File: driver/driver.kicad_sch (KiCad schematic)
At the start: 16 parts, among them U1 ULN2003A, U2 ULN2003A, U3 74HC595, U4 74HC165

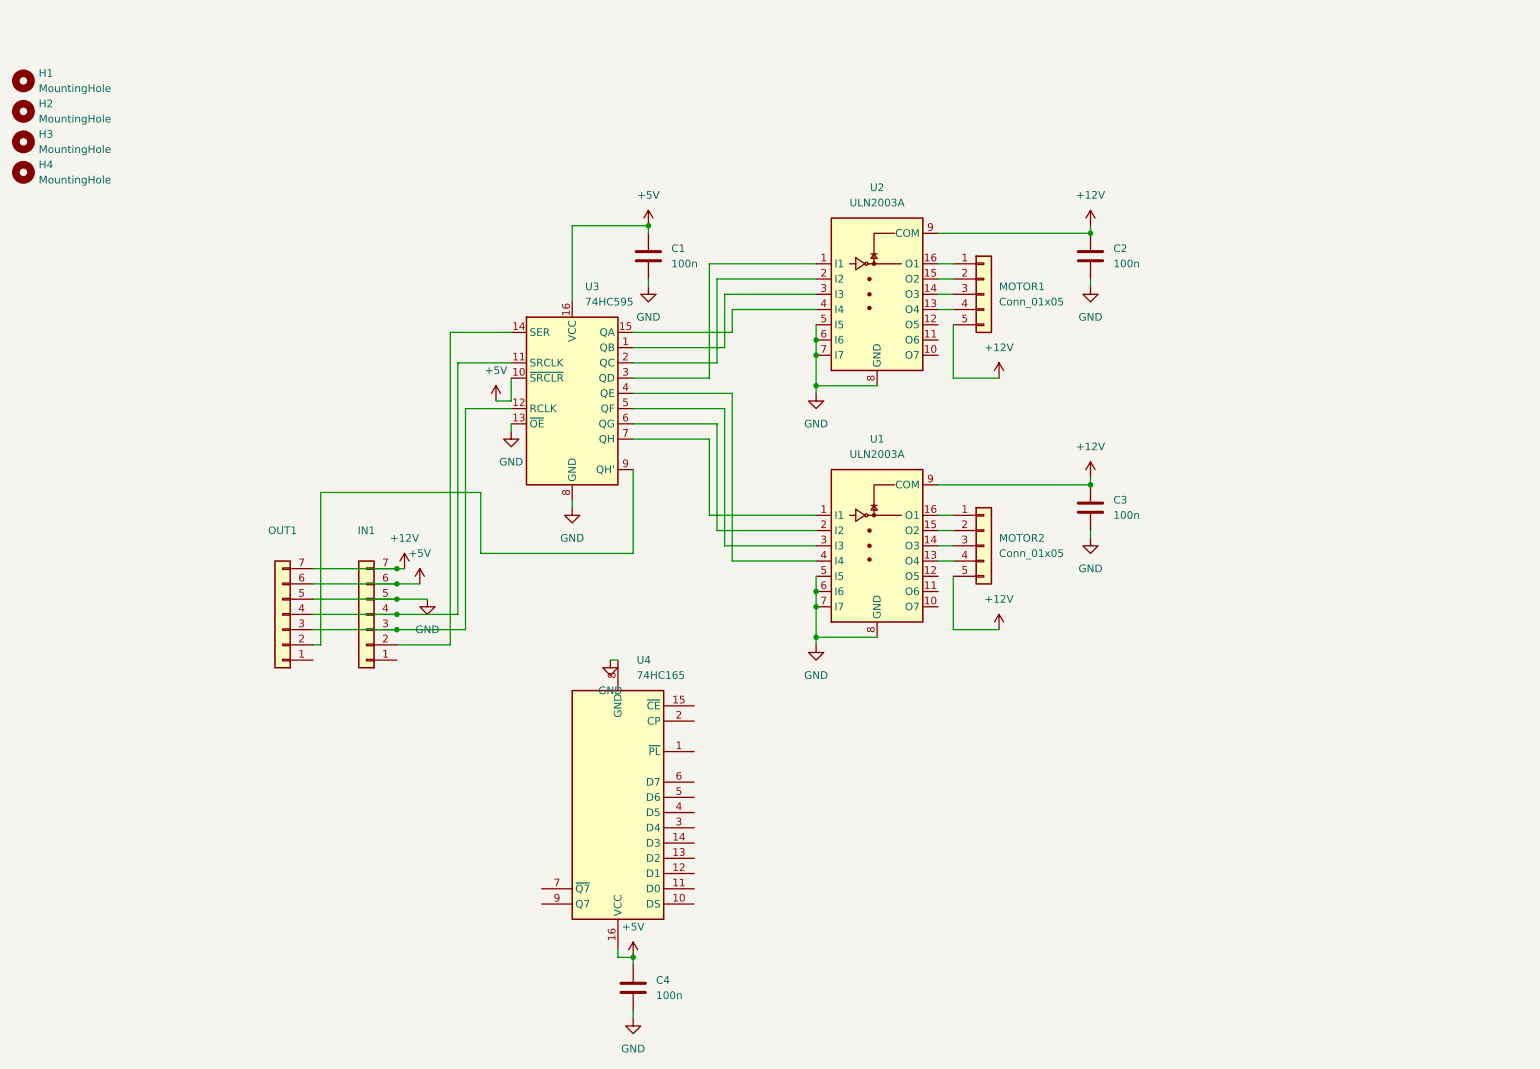
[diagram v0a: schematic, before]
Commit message: Start to implement controller and driver.
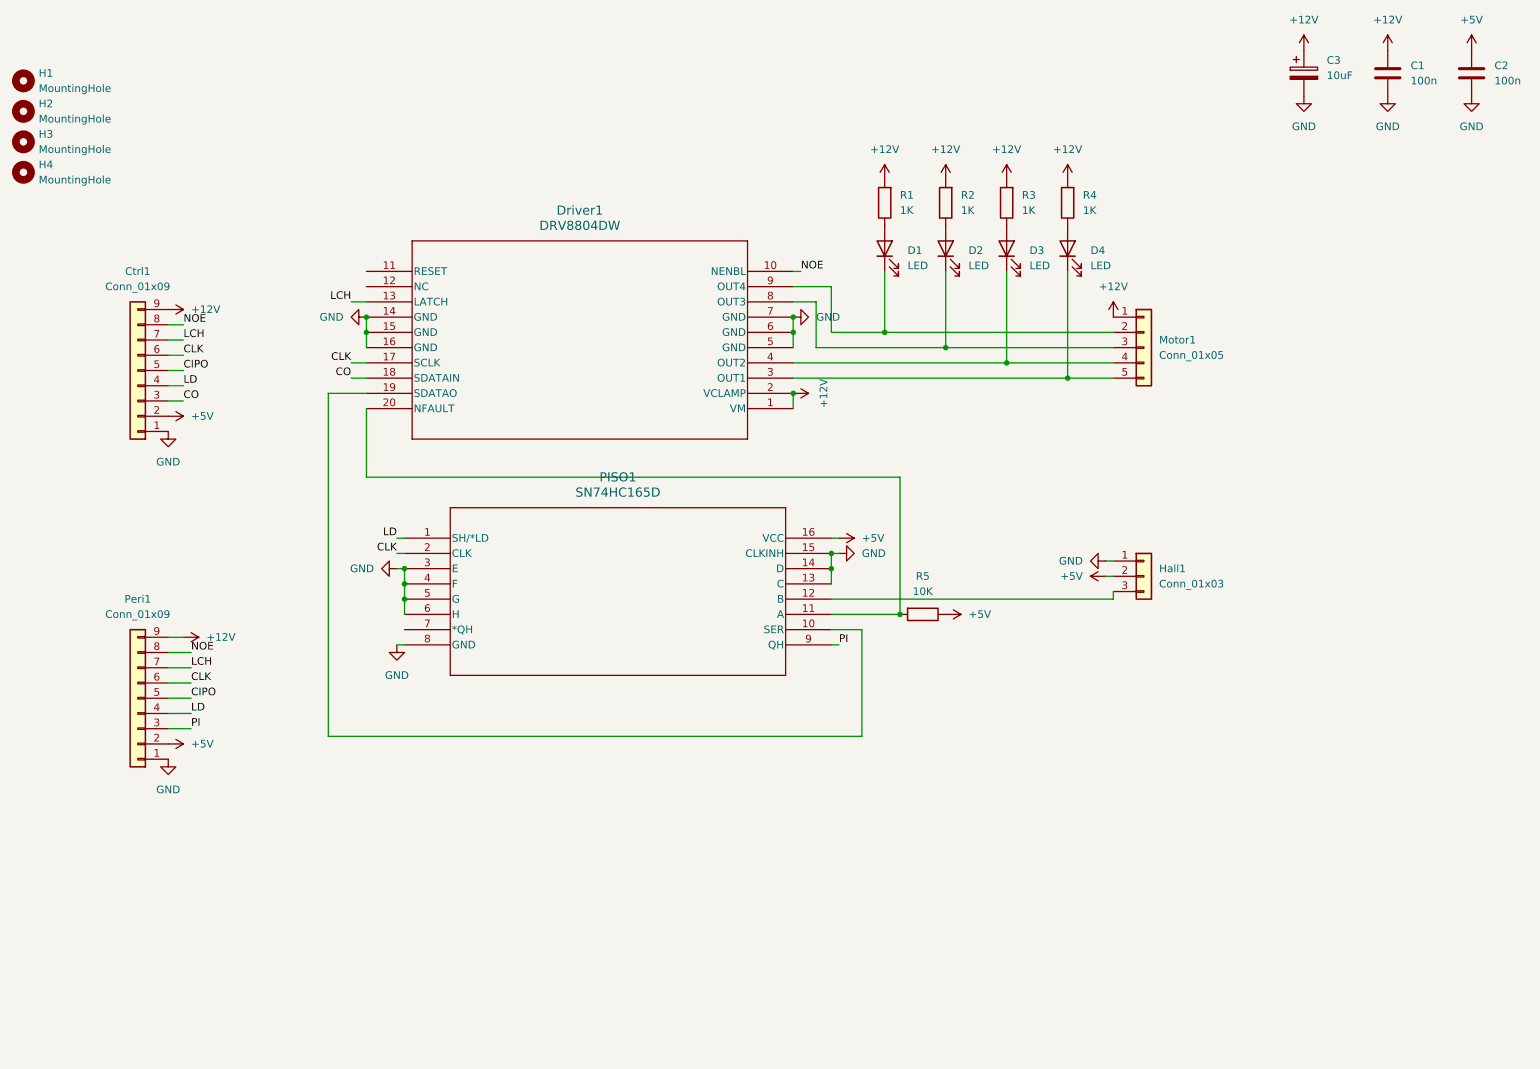
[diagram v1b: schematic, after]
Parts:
- removed C2, C3, C4: 100n, Capacitor_SMD:C_0805_2012Metric, symbol Device:C
- removed IN1, OUT1: ~, Connector_JST:JST_XH_B7B-XH-A_1x07_P2.50mm_Vertical, symbol Connector_Generic:Conn_01x07
- removed MOTOR2: Conn_01x05, Connector_JST:JST_XH_B5B-XH-A_1x05_P2.50mm_Vertical, symbol Connector_Generic:Conn_01x05
- removed U1, U2: ULN2003A, Package_DIP:DIP-16_W7.62mm_Socket, symbol Transistor_Array:ULN2003A
- removed U3: 74HC595, Package_SO:TSSOP-16_4.4x5mm_P0.65mm, symbol 74xx:74HC595
- removed U4: 74HC165, Package_SO:TSSOP-16_4.4x5mm_P0.65mm, symbol 74xx:74HC165
- added C1: 100n, Capacitor_SMD:C_0805_2012Metric, symbol Device:C
- added C3: 10uF, Capacitor_SMD:C_0805_2012Metric, symbol Device:C_Polarized
- added Ctrl1, Peri1: Conn_01x09, Connector_JST:JST_XH_B9B-XH-A_1x09_P2.50mm_Vertical, symbol Connector_Generic:Conn_01x09
- added D1, D2, D3, D4: LED, LED_SMD:LED_0603_1608Metric, symbol Device:LED
- added Driver1: DRV8804DW, DW20, symbol DRV8804:DRV8804DW
- added Hall1: Conn_01x03, Connector_PinSocket_2.54mm:PinSocket_1x03_P2.54mm_Vertical, symbol Connector_Generic:Conn_01x03
- added PISO1: SN74HC165D, D16, symbol SN74HCS165:SN74HC165D
- added R1, R2, R3, R4: 1K, Resistor_SMD:R_0603_1608Metric, symbol Device:R
- added R5: 10K, Resistor_SMD:R_0603_1608Metric, symbol Device:R
- H1, H2, H3, H4: footprint MountingHole:MountingHole_3.7mm -> MountingHole:MountingHole_2.2mm_M2_ISO14580
- renumbered C1 to C2, MOTOR1 to Motor1
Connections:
- net +12V: now also Motor1.1 (Pin_1), C1.1, C3.1, Ctrl1.9 (Pin_9), Driver1.1 (VM), Driver1.2 (VCLAMP), Peri1.9 (Pin_9), R1.2, R2.2, R3.2, R4.2; no longer Motor1.5 (Pin_5)
- net +5V: now also Ctrl1.2 (Pin_2), Hall1.2 (Pin_2), PISO1.16 (VCC), Peri1.2 (Pin_2), R5.1
- net GND: now also C1.2, C3.2, Ctrl1.1 (Pin_1), Driver1.14 (GND), Driver1.15 (GND), Driver1.16 (GND), Driver1.5 (GND), Driver1.6 (GND), Driver1.7 (GND), Hall1.1 (Pin_1), PISO1.13 (C), PISO1.14 (D), PISO1.15 (CLKINH), PISO1.3 (E), PISO1.4 (F), PISO1.5 (G), PISO1.6 (H), PISO1.8 (GND), Peri1.1 (Pin_1)
- net at Motor1.2 (Pin_2): now also D1.1 (K), Driver1.9 (OUT4)
- net at Motor1.3 (Pin_3): now also D2.1 (K), Driver1.8 (OUT3)
- net at Motor1.4 (Pin_4): now also D3.1 (K), Driver1.4 (OUT2)
- new net: Driver1.20 (NFAULT), PISO1.11 (A), R5.2
- new net: D4.1 (K), Driver1.3 (OUT1), Motor1.5 (Pin_5)
- new net: D4.2 (A), R4.1
- new net: Hall1.3 (Pin_3), PISO1.12 (B)
- new net: Driver1.19 (SDATAO), PISO1.10 (SER)
- new net: D1.2 (A), R1.1
- new net: D2.2 (A), R2.1
- new net: D3.2 (A), R3.1
- new net CIPO: Ctrl1.5 (Pin_5), Peri1.5 (Pin_5)
- new net CLK: Ctrl1.6 (Pin_6), Driver1.17 (SCLK), PISO1.2 (CLK), Peri1.6 (Pin_6)
- new net CO: Ctrl1.3 (Pin_3), Driver1.18 (SDATAIN)
- new net LCH: Ctrl1.7 (Pin_7), Driver1.13 (LATCH), Peri1.7 (Pin_7)
- new net LD: Ctrl1.4 (Pin_4), PISO1.1 (SH/*LD), Peri1.4 (Pin_4)
- new net NOE: Ctrl1.8 (Pin_8), Driver1.10 (NENBL), Peri1.8 (Pin_8)
- new net PI: PISO1.9 (QH), Peri1.3 (Pin_3)
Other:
- moved on the sheet: C2, Motor1
